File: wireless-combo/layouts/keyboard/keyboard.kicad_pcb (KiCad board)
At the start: 2 copper layers, 36 x 12.2 mm, 2 parts

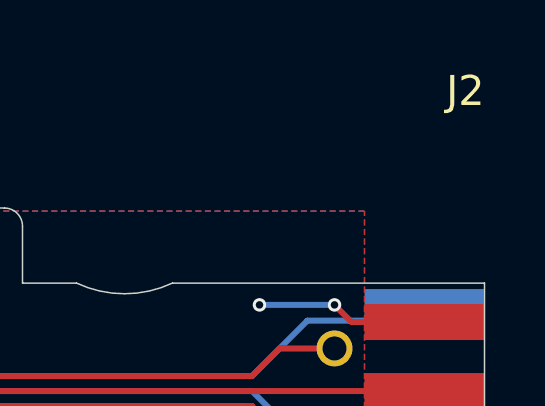
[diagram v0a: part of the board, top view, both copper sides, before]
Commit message: wireless-combo: タイトル / リビジョンを設定し、v1.0.0 製造データを生成
- 3 基板の KiCad title_block に TITLE / REVISION (v1.0.0) を設定し、
  シルクの版数表記を ${REVISION} 参照に変更
    default  = MimicX-combo
    joystick = MimicX-breakout-atari-joystick
    keyboard = MimicX-breakout-x68000-keyboard
- Fabrication Toolkit の ARCHIVE_NAME を ${TITLE}_${REVISION} にして
  production/ (Gerber zip / BOM / CPL / netlist) を生成
- default: solder_mask_to_copper_clearance 0.005
- keyboard: J2 (Mini DIN) のリファレンス表示を非表示

Co-Authored-By: Claude Opus 5.5 <noreply@anthropic.com>
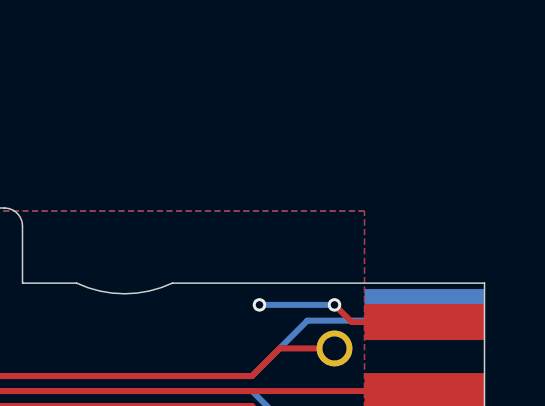
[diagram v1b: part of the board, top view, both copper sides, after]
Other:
- board text added: "${REVISION} by @kunichiko"
- board text removed: "v1.0.0 by @kunichiko"
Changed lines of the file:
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@@
 	)
 	(paper "A4")
+	(title_block
+		(title "MimicX-breakout-x68000-keyboard")
+		(rev "v1.0.0")
+	)
 	(layers
 		(0 "F.Cu" signal)
@@
 			(at 0 -10 0)
 			(layer "F.SilkS")
+			(hide yes)
 			(effects
 				(font
@@
 		)
 	)
-	(gr_text "v1.0.0 by @kunichiko"
+	(gr_text "${REVISION} by @kunichiko"
 		(at 156.8128 96 270)
 		(layer "F.SilkS")

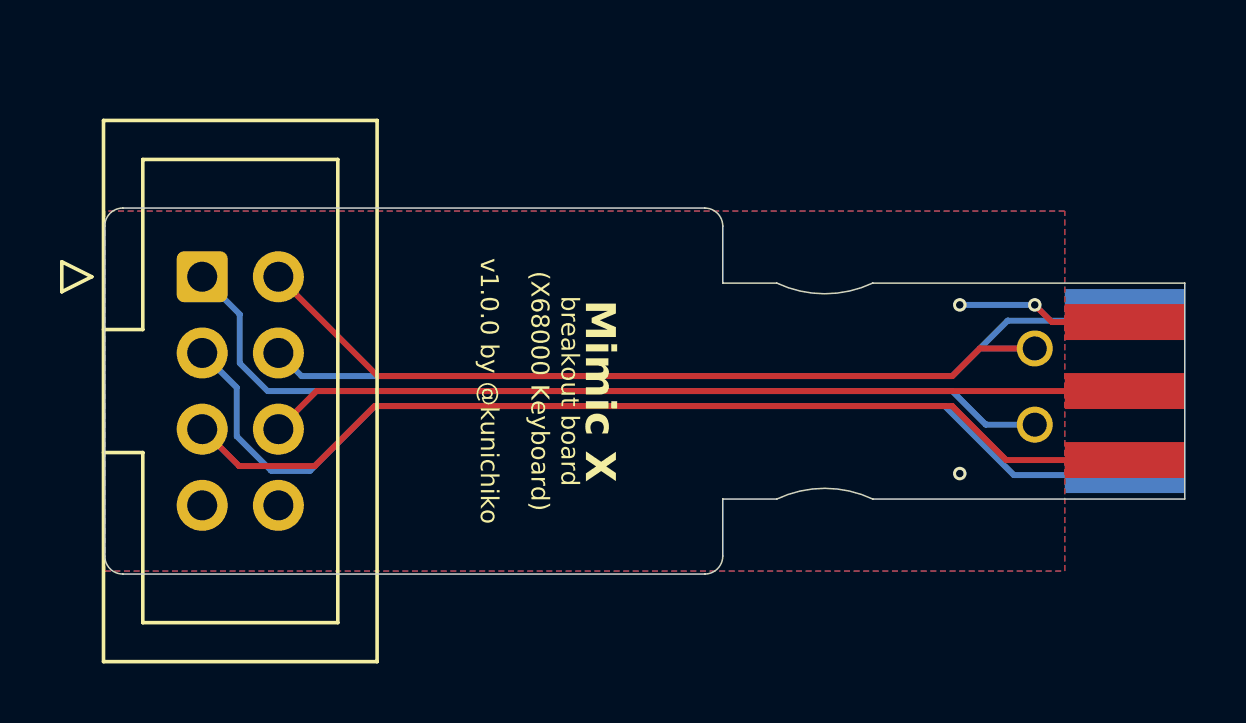
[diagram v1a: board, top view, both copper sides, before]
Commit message: wireless-combo: 版数をプロジェクト変数 BOARD_REV に移す
atopile 0.15.9 の PCB パーサは title_block の (rev ...) を "revision" として
読むため取りこぼし、ato build のたびに rev が消えてシルクの ${REVISION} が
空になる。版数は atopile が触らない .kicad_pro のテキスト変数 BOARD_REV に
置き、シルクと Fabrication Toolkit の ARCHIVE_NAME はそれを参照する
(ARCHIVE_NAME はプラグインが ExpandTextVars でプロジェクト変数まで展開する)。
title_block の rev は図面枠用に残すが、正は BOARD_REV。

3 基板とも ato build 後に BOARD_REV と ${BOARD_REV} 参照が残り、
シルクが v1.0.0 と描画されることを作業コピーで確認済み。

Co-Authored-By: Claude Opus 5.5 <noreply@anthropic.com>
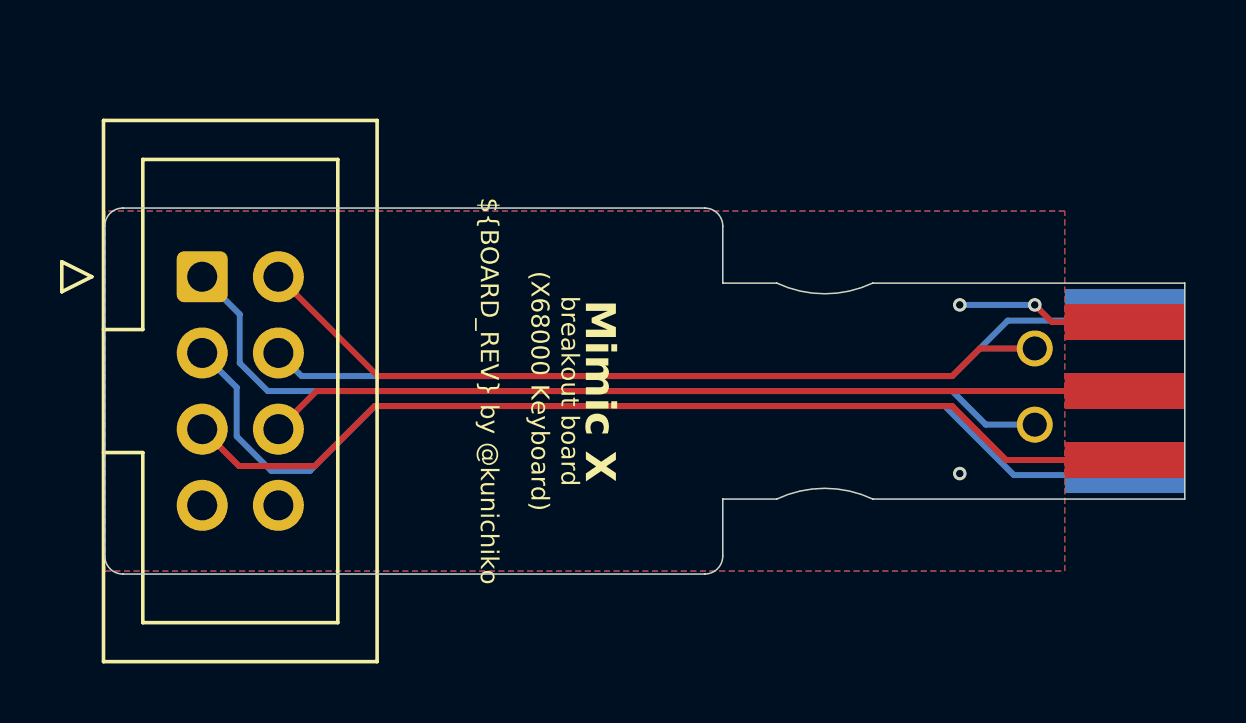
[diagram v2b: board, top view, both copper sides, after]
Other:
- board text added: "${BOARD_REV} by @kunichiko"
- board text removed: "${REVISION} by @kunichiko"
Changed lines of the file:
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@@
 		)
 	)
-	(gr_text "${REVISION} by @kunichiko"
+	(gr_text "${BOARD_REV} by @kunichiko"
 		(at 156.8128 96 270)
 		(layer "F.SilkS")
